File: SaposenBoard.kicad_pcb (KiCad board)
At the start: 2 copper layers, 60 x 50 mm, 70 parts, among them IC1 BSO220, IC2 BSO220, IC3 BSO220, IC4 BSO220, J1 ADC4ch, J2 Extra2ch+LED, J3 Encoder1, J4 Encoder2, J5 I2C, J6 Battery, J7 Motor1, J8 Motor2, Q2 IRLML6344, SW1 BatterySW, SW2 SW_Push, SW3 SW_Push, U1 A4955GLPTR-T, U2 A4955GLPTR-T, U3 MPU-6500, U4 NUCLEO-F303K8

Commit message: [update]終わった
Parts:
- moved R22 33.8 mm to (121.1, 89.9)
- moved D1 25.0 mm to (128.9, 70.9), turned to 90 degrees
- moved R24 11.9 mm to (122.7, 89.9), turned to -90 degrees
- moved R2 11.2 mm to (122.7, 76.7), turned to -90 degrees
- moved R4 11.2 mm to (121.1, 76.7), turned to 90 degrees
- moved R25 10.9 mm to (122.7, 93.0)
- moved R23 7.98 mm to (121.1, 93.0)
- moved Q2 5.50 mm to (130.1, 83.3), turned to 0 degrees
- moved R7 2.80 mm to (130.1, 79.2)
- moved R8 0.40 mm to (130.1, 80.8)
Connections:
- J2 pad 2: NUCLEO_LED -> Extra1
- J2 pad 3: Extra1 -> Extra2
- J2 pad 4: Extra2 -> NUCLEO_LED
- U4 pad 3_1: ENC1_2 -> MOT1_IN2
- U4 pad 3_12: ENC1_1 -> MOT2_IN2
- U4 pad 3_13: MOT1_IN2 -> MOT2_IN1
- U4 pad 3_14: ENC2_1 -> Extra2
- U4 pad 3_15: ENC2_2 -> Extra1
- U4 pad 3_6: VBAT -> ADC4
- U4 pad 3_9: Extra1 -> ADC3
- U4 pad 4_10: ADC1 -> ADC2
- U4 pad 4_11: MOT2_IN2 -> ENC1_1
- U4 pad 4_12: MOT2_IN1 -> ADC1
- U4 pad 4_6: Extra2 -> ENC2_2
- U4 pad 4_7: ADC4 -> ENC2_1
- U4 pad 4_8: ADC3 -> ENC1_2
- U4 pad 4_9: ADC2 -> VBAT
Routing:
- net +5V: track 79.0 -> 53.3 mm
- net ENC1_2: track 61.5 -> 36.6 mm, vias 0 -> 1
- net +BATT: track 137.4 -> 118.1 mm, vias 9 -> 11
- net GND: track 309.4 -> 292.4 mm, vias 145 -> 180
- net ADC4: track 33.7 -> 50.5 mm, vias 0 -> 1
- net ADC3: track 33.3 -> 49.0 mm, vias 0 -> 1
- net MOT2_IN2: track 31.4 -> 46.3 mm, vias 0 -> 2
- net MOT2_IN1: track 34.2 -> 48.5 mm, vias 0 -> 2
- net ENC2_2: track 25.2 -> 38.3 mm, vias 0 -> 1
- net ENC2_1: track 24.1 -> 33.5 mm, vias 0 -> 1
- net Extra1: track 40.7 -> 35.2 mm
- net SCLK: track 74.8 -> 70.6 mm
- net ENC1_1: track 31.0 -> 26.9 mm, vias 0 -> 1
- net Net-(BZ1-Pad2): track 26.6 -> 22.5 mm
- net ADC1: track 32.7 -> 28.9 mm
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- added copper zone on F.Cu, net +BATT

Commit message: a
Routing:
- net GND: vias 180 -> 158

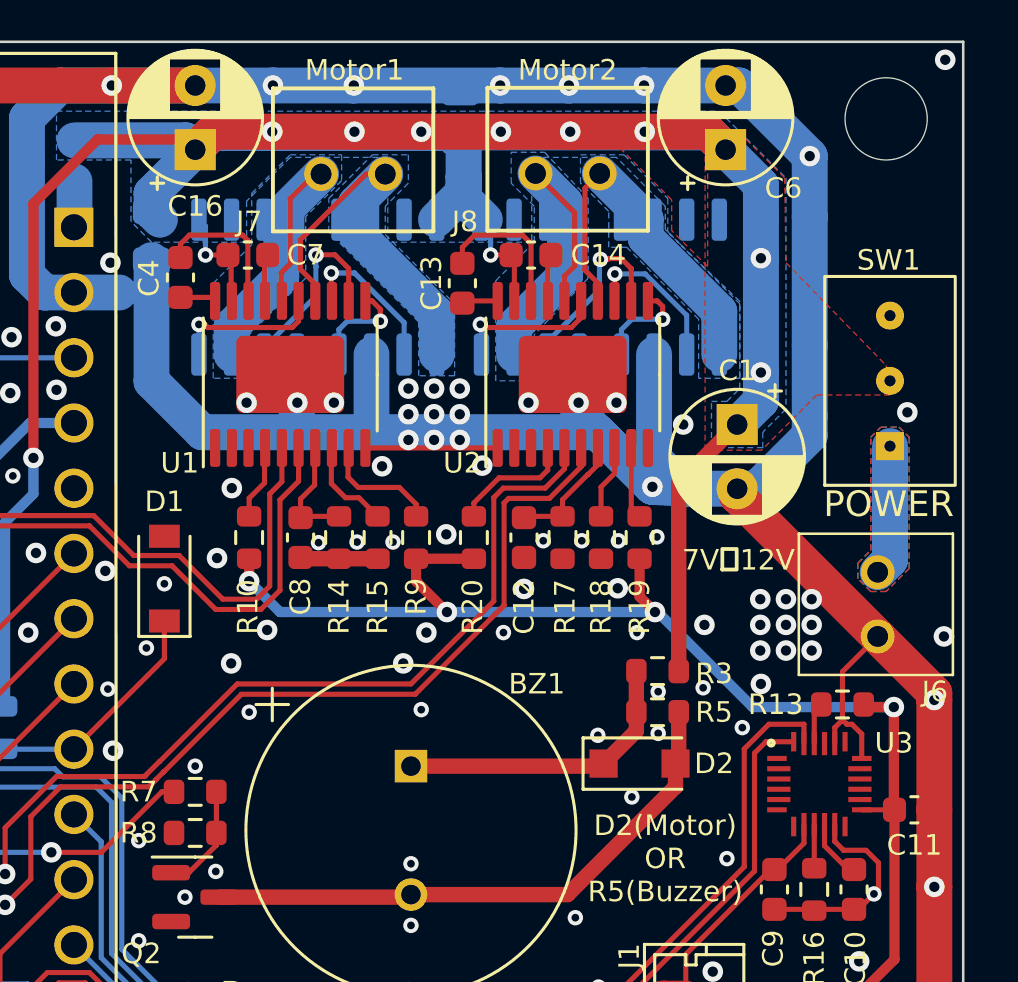
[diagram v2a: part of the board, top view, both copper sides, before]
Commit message: [fix]コネクタの向きを修正
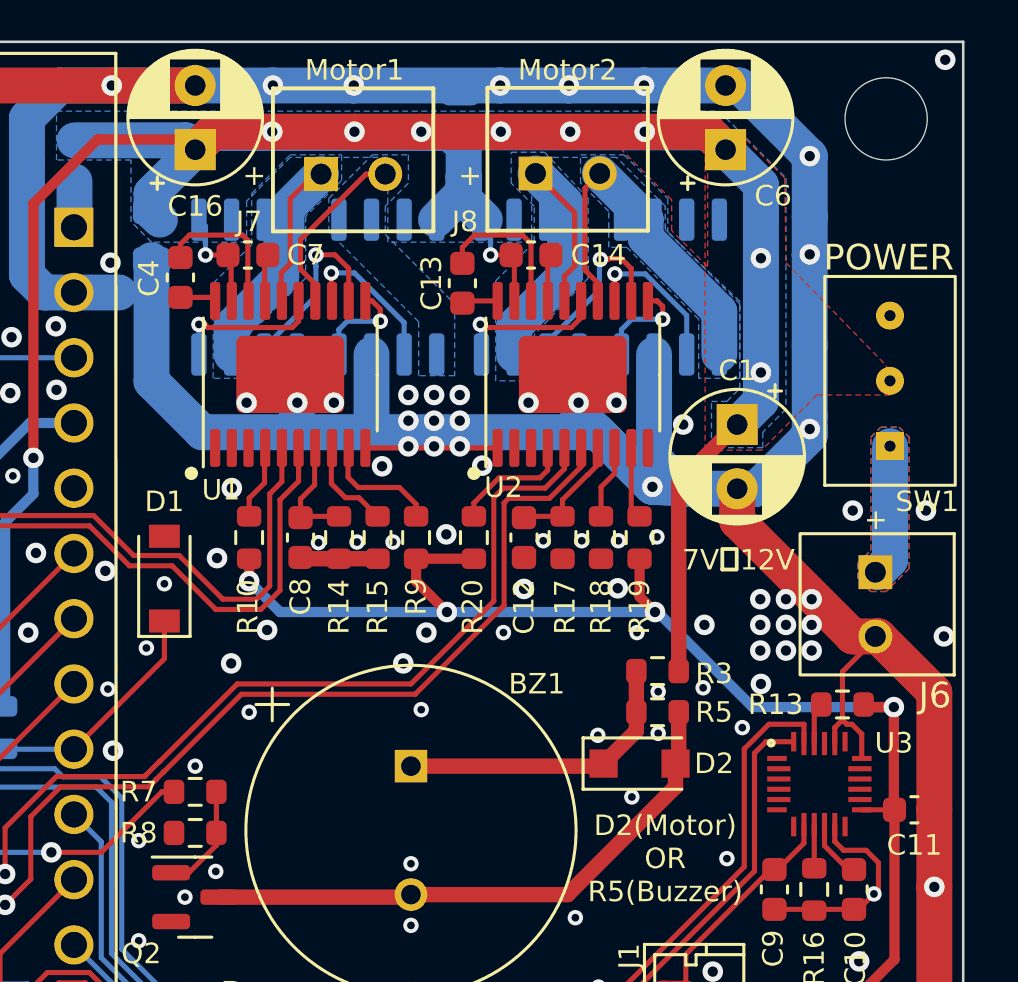
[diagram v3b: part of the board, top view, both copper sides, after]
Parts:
- moved J6 0.05 mm to (156.7, 71.9), turned to -90 degrees
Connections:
- J6 pad 1: GND -> Net-(J6-Pad1)
- J6 pad 2: Net-(J6-Pad2) -> GND
- SW1 pad 1: Net-(J6-Pad2) -> Net-(J6-Pad1)
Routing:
- net Net-(IC2-Pad1): track 15.6 -> 6.82 mm
- net Net-(J6-Pad2): track 5.11 -> 0.00 mm
- net Net-(J6-Pad1): track 0.00 -> 5.11 mm
- net GND: track 292.4 -> 293.0 mm, vias 158 -> 160
- added copper zone on B.Cu, net Net-(J6-Pad1)
- added copper zone on F.Cu, net Net-(J6-Pad1)
- removed copper zone on B.Cu, net Net-(J6-Pad2)
- removed copper zone on F.Cu, net Net-(J6-Pad2)
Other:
- board text added: "+"

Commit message: V1.0
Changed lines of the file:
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@@
     )
     (fp_rect (start -4.065 -2.54) (end 4.065 2.54) (layer "F.SilkS") (width 0.12) (fill none))
-    (pad "1" thru_hole rect (at -2.54 0 90) (size 1.09 1.09) (drill 0.43) (layers *.Cu *.Mask)
+    (pad "1" thru_hole rect (at -2.54 0 90) (size 1.6 1.6) (drill 0.8) (layers *.Cu *.Mask)
       (net 65 "Net-(J6-Pad1)") (pintype "passive"))
-    (pad "2" thru_hole circle (at 0 0 90) (size 1.09 1.09) (drill 0.43) (layers *.Cu *.Mask)
+    (pad "2" thru_hole circle (at 0 0 90) (size 1.6 1.6) (drill 0.8) (layers *.Cu *.Mask)
       (net 3 "+BATT") (pintype "passive"))
-    (pad "3" thru_hole circle (at 2.54 0 90) (size 1.09 1.09) (drill 0.43) (layers *.Cu *.Mask))
+    (pad "3" thru_hole circle (at 2.54 0 90) (size 1.6 1.6) (drill 0.8) (layers *.Cu *.Mask))
   )
   (footprint "Footprints:CONN_B02B-PASKLFSN_JST" (layer "F.Cu")
@@
   (via (at 104.95 88.45) (size 0.8) (drill 0.4) (layers "F.Cu" "B.Cu") (free) (net 4))
   (via (at 121.425 99.2) (size 0.8) (drill 0.4) (layers "F.Cu" "B.Cu") (free) (net 4))
-  (via (at 154.025 65.075) (size 0.8) (drill 0.4) (layers "F.Cu" "B.Cu") (net 4))
+  (via (at 154.025 65.325) (size 0.8) (drill 0.4) (layers "F.Cu" "B.Cu") (net 4))
   (via (at 154.1 71.7) (size 0.8) (drill 0.4) (layers "F.Cu" "B.Cu") (free) (net 4))
   (via (at 107.6 85.975) (size 0.8) (drill 0.4) (layers "F.Cu" "B.Cu") (free) (net 4))
@@
   (via (at 132.9 72.9) (size 0.8) (drill 0.4) (layers "F.Cu" "B.Cu") (free) (net 4))
   (segment (start 149.127443 67.4) (end 151.2 67.4) (width 1.4) (layer "B.Cu") (net 4))
+  (segment (start 154.025 65.325) (end 151.95 67.4) (width 1.4) (layer "B.Cu") (net 4))
   (segment (start 128.4 63.221366) (end 130.378634 65.2) (width 1.4) (layer "B.Cu") (net 4))
   (segment (start 145.025 64.05) (end 145.025 64.45) (width 1.4) (layer "B.Cu") (net 4))
@@
   (segment (start 154.025 56.825) (end 154.025 58.275) (width 1.4) (layer "B.Cu") (net 4))
   (segment (start 130.378634 65.2) (end 136.9 65.2) (width 1.4) (layer "B.Cu") (net 4))
+  (segment (start 151.95 67.4) (end 151.2 67.4) (width 1.4) (layer "B.Cu") (net 4))
   (segment (start 136.275 51.7) (end 133.125 51.7) (width 1.4) (layer "B.Cu") (net 4))
   (segment (start 150.75 51.7) (end 147.575 51.7) (width 1.4) (layer "B.Cu") (net 4))
   (segment (start 124.235 59.76) (end 125.3775 59.76) (width 1.4) (layer "B.Cu") (net 4))
   (segment (start 130.1 51.7) (end 124.825 51.7) (width 1.4) (layer "B.Cu") (net 4))
-  (segment (start 154.025 65.075) (end 154.025 65.325) (width 1.4) (layer "B.Cu") (net 4))
-  (segment (start 154.025 61.825) (end 154.025 64.575) (width 1.4) (layer "B.Cu") (net 4))
   (segment (start 144.65 51.7) (end 141.975 51.7) (width 1.4) (layer "B.Cu") (net 4))
   (segment (start 147.9 67.325) (end 149.127443 67.4) (width 1.4) (layer "B.Cu") (net 4))
@@
   (segment (start 145.775 65.2) (end 147.9 67.325) (width 1.4) (layer "B.Cu") (net 4))
   (segment (start 104.504511 71.295489) (end 104.4 71.4) (width 0.4) (layer "B.Cu") (net 4))
+  (segment (start 154.025 65.325) (end 154.025 58.275) (width 1.4) (layer "B.Cu") (net 4))
   (segment (start 154.025 54.45) (end 154.025 56.825) (width 1.4) (layer "B.Cu") (net 4))
-  (segment (start 154.025 64.575) (end 154.025 65.075) (width 1.4) (layer "B.Cu") (net 4))
   (segment (start 125.3775 59.76) (end 127.14 59.76) (width 1.4) (layer "B.Cu") (net 4))
   (segment (start 151.275 51.7) (end 154.025 54.45) (width 1.4) (layer "B.Cu") (net 4))
@@
   (segment (start 145.055 64.02) (end 145.055 62.175) (width 1.4) (layer "B.Cu") (net 4))
   (segment (start 123.55 52.975) (end 123.55 54.725) (width 1.4) (layer "B.Cu") (net 4))
-  (segment (start 154.025 58.325) (end 154.025 61.825) (width 1.4) (layer "B.Cu") (net 4))
-  (segment (start 154.025 58.275) (end 154.025 58.325) (width 1.4) (layer "B.Cu") (net 4))
-  (segment (start 151.95 67.4) (end 151.2 67.4) (width 1.4) (layer "B.Cu") (net 4))
   (segment (start 123.55 59.075) (end 124.235 59.76) (width 1.4) (layer "B.Cu") (net 4))
-  (segment (start 154.025 65.325) (end 151.95 67.4) (width 1.4) (layer "B.Cu") (net 4))
   (segment (start 128.4 58.5) (end 128.4 63.221366) (width 1.4) (layer "B.Cu") (net 4))
   (segment (start 134.055 62.1) (end 134.055 64.03) (width 1.4) (layer "B.Cu") (net 4))
@@
         (xy 153.05 55.3)
         (xy 153.1 58.6)
-        (xy 157 62.6)
-        (xy 157.15 63.75)
-        (xy 154.3 63.75)
+        (xy 157.15 62.2)
+        (xy 157.15 64.225)
+        (xy 154.3 64.225)
         (xy 152.15 65.9)
         (xy 149.95 65.9)

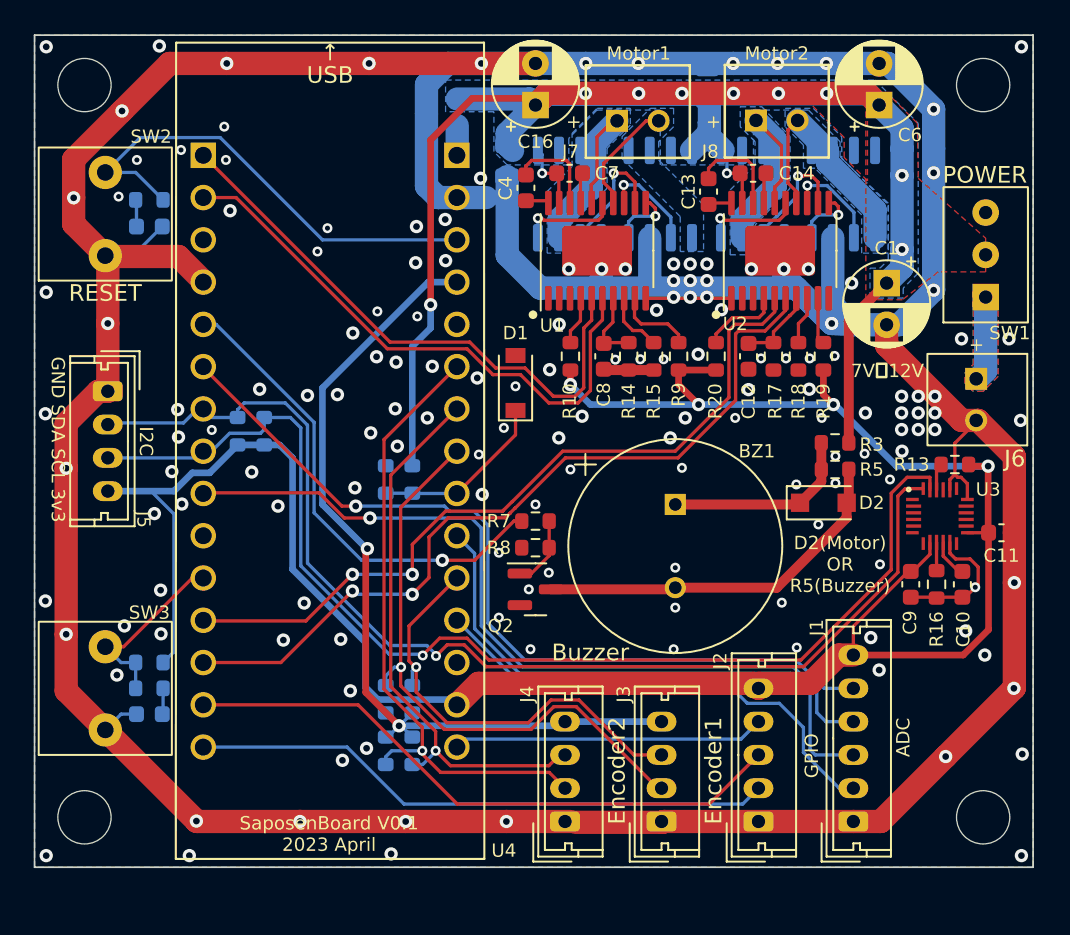
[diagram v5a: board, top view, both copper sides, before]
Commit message: [fix]IMUを裏に移動
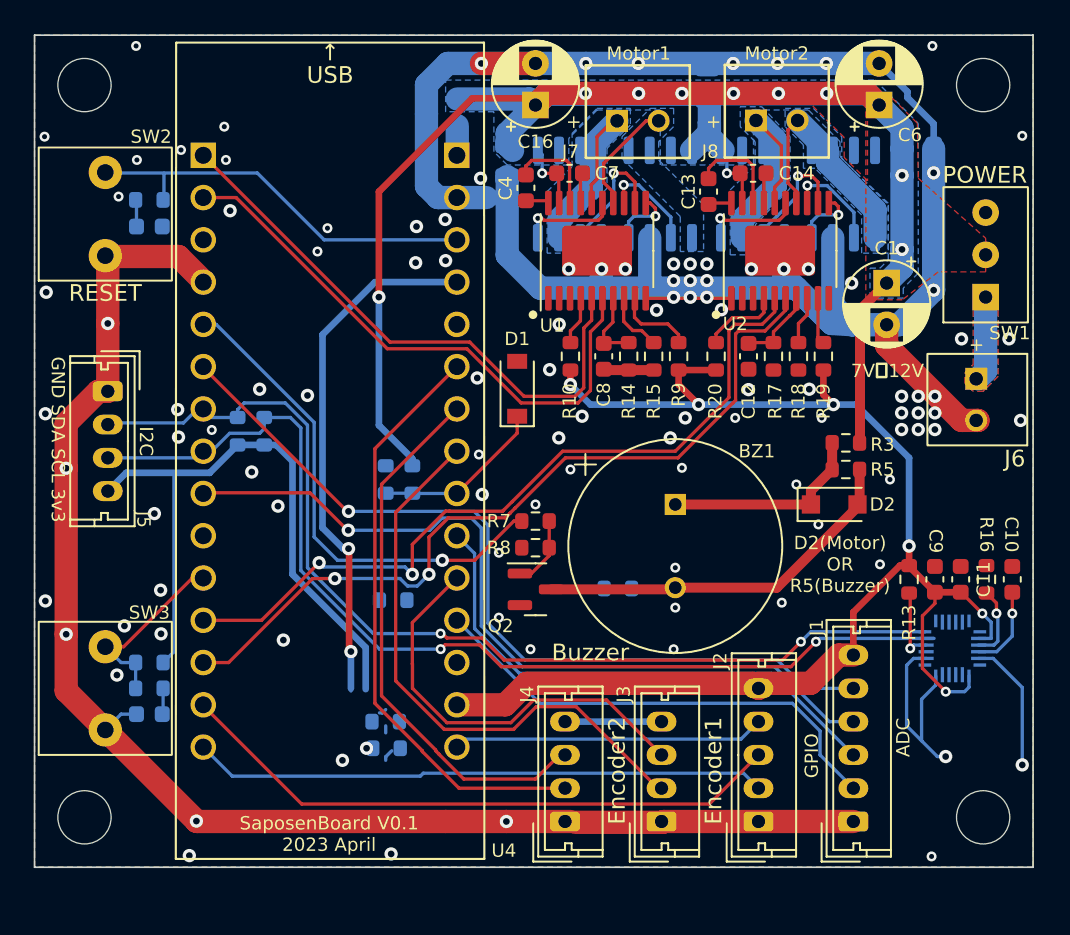
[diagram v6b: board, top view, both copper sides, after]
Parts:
- REF** (x4): footprint MountingHole:MountingHole_3.2mm_M3 -> Footprints:MountingHole_3.2mm_M3
- U3: moved to B.Cu
- moved R22 15.5 mm to (135.1, 83.2), turned to 0 degrees
- moved U3 7.99 mm to (155.2, 86.8), turned to -90 degrees
- moved R13 7.43 mm to (152.6, 82.7), turned to -90 degrees
- moved R24 6.06 mm to (121.5, 84.0), turned to 0 degrees
- moved C11 3.72 mm to (155.7, 82.7), turned to 90 degrees
- moved C10 3.01 mm to (158.8, 82.7), turned to 90 degrees
- moved R16 3.01 mm to (157.2, 82.7), turned to -90 degrees
- moved R23 1.75 mm to (121.1, 91.2), turned to 0 degrees
- moved R25 1.56 mm to (121.2, 92.8), turned to 0 degrees
- moved C9 1.48 mm to (154.1, 82.7), turned to 90 degrees
- moved D2 0.66 mm to (148.1, 78.2)
- moved R3 0.65 mm to (148.8, 74.5)
- moved R5 0.65 mm to (148.8, 76.1)
- moved D1 0.36 mm to (129.0, 71.2)
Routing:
- net GND: track 293.0 -> 230.6 mm, vias 160 -> 110
- net +3V3: track 138.4 -> 125.8 mm, vias 4 -> 6
- net +5V: track 53.3 -> 43.0 mm
- net SCLK: track 70.6 -> 63.2 mm, vias 1 -> 2
- net SDA: track 69.4 -> 62.5 mm, vias 1 -> 2
- net NRST: track 28.8 -> 24.5 mm
- net Net-(R13-Pad2): track 1.64 -> 4.39 mm, vias 0 -> 1
- net Net-(R16-Pad2): track 1.70 -> 4.42 mm, vias 0 -> 1
- net Net-(C10-Pad1): track 2.35 -> 5.05 mm, vias 0 -> 1
- net ADC2: track 33.9 -> 31.9 mm
- net ENC2_2: track 38.3 -> 36.6 mm, vias 1 -> 0
- net ENC1_2: track 36.6 -> 35.1 mm, vias 1 -> 0
- net ENC1_1: track 26.9 -> 25.5 mm, vias 1 -> 0
- net +BATT: track 118.1 -> 119.5 mm
- net SPEAKER: track 29.2 -> 30.0 mm
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
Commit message: [add]なんか足した
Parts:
- removed R5: 1k, Resistor_SMD:R_0603_1608Metric
- C10, C11, C9: value 100n -> 0.1u; moved to B.Cu
- C2, C3: value 100n -> 0.1u; moved to F.Cu
- FB1, R1, R11, R12, R2, R21, R22, R23, R24, R25, R4, R6: moved to F.Cu
- R13, R16: moved to B.Cu
- moved U3 41.2 mm to (115.6, 75.4)
- moved C10 38.4 mm to (120.8, 77.0), turned to 0 degrees
- moved R16 37.1 mm to (120.8, 75.4), turned to 180 degrees
- moved C11 35.1 mm to (120.8, 78.5), turned to 0 degrees
- moved C9 34.5 mm to (120.8, 73.9), turned to 0 degrees
- moved R13 33.4 mm to (120.8, 72.4), turned to 180 degrees
- moved Q2 27.8 mm to (157.6, 87.4), turned to 90 degrees
- moved R25 27.5 mm to (148.0, 86.6), turned to 90 degrees
- moved R23 25.8 mm to (146.4, 86.6), turned to 90 degrees
- moved R24 23.5 mm to (144.9, 86.6), turned to 90 degrees
- moved R8 23.2 mm to (152.5, 86.6), turned to 90 degrees
- moved R19 20.9 mm to (135.8, 86.6)
- moved R7 20.7 mm to (149.5, 86.6), turned to 90 degrees
- moved R15 19.5 mm to (128.1, 86.6)
- moved R9 19.5 mm to (129.7, 86.6)
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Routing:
- net GND: track 230.6 -> 0.00 mm, vias 110 -> 0
- net +3V3: track 125.8 -> 0.00 mm, vias 6 -> 0
- net +BATT: track 119.5 -> 2.73 mm, vias 11 -> 0
- net SCLK: track 63.2 -> 0.00 mm, vias 2 -> 0
- net SDA: track 62.5 -> 0.00 mm, vias 2 -> 0
- net ADC4: track 50.5 -> 0.00 mm, vias 1 -> 0
- net ADC3: track 48.8 -> 0.00 mm, vias 1 -> 0
- net MOT2_IN1: track 48.5 -> 0.00 mm, vias 2 -> 0
- net MOT2_IN2: track 46.8 -> 0.00 mm, vias 2 -> 0
- net +5V: track 43.0 -> 0.00 mm, vias 2 -> 0
- net Extra2: track 37.1 -> 0.00 mm
- net ENC2_2: track 36.6 -> 0.00 mm
- net ENC1_2: track 35.1 -> 0.00 mm
- net MOT1_IN2: track 34.6 -> 0.00 mm
- net Extra1: track 34.5 -> 0.00 mm
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- removed copper zone on B.Cu, net +BATT
- removed copper zone on F.Cu, net +BATT
- removed copper zone on B.Cu, net GND
- removed copper zone on F.Cu, net GND
- removed copper zone on B.Cu, net Net-(IC1-Pad3)
- removed copper zone on B.Cu, net Net-(IC2-Pad1)
- removed copper zone on B.Cu, net Net-(IC3-Pad3)
- removed copper zone on B.Cu, net Net-(IC4-Pad1)
- removed copper zone on B.Cu, net Net-(J6-Pad1)
- removed copper zone on F.Cu, net Net-(J6-Pad1)
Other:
- board text added: "SaposenBoard V0.2 2023 May"
- board text removed: "7V～12V"
- board text removed: "D2(Motor) OR R5(Buzzer)"
- board text removed: "SaposenBoard V0.1 2023 April"
